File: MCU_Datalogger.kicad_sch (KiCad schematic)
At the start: 0 parts

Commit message: Have added required symbols to schematic sheets
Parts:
- added BT1: Battery, symbol Device:Battery
- added C1, C2, C3, C4: C, symbol Device:C
- added C5: C_Polarized_US, symbol Device:C_Polarized_US
- added D1, D2: LED, symbol Device:LED
- added H1, H2, H3, H4: MountingHole, symbol Mechanical:MountingHole
- added R1, R2, R3, R4, R5, R6, R7: R_US, symbol Device:R_US
- added U1, U2: 24LC1025, symbol Memory_EEPROM:24LC1025
- added U3: ATMEGA328P-AU, ATMEGA328P-AU:QFP80P900X900X120-32N, symbol ATMEGA328P-AU:ATMEGA328P-AU
- added U4: DS1337S_, DS1337S_:SOIC127P600X175-8N, symbol DS1337S_:DS1337S_
- added Y1, Y2: Crystal, symbol Device:Crystal
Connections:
- new net: U3.21 (GND), U3.3 (GND), U3.5 (GND)
- new net: U3.4 (VCC), U3.6 (VCC)
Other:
- added sheet Connectors (connectors.kicad_sch)
- title: (none) -> ${project_name}

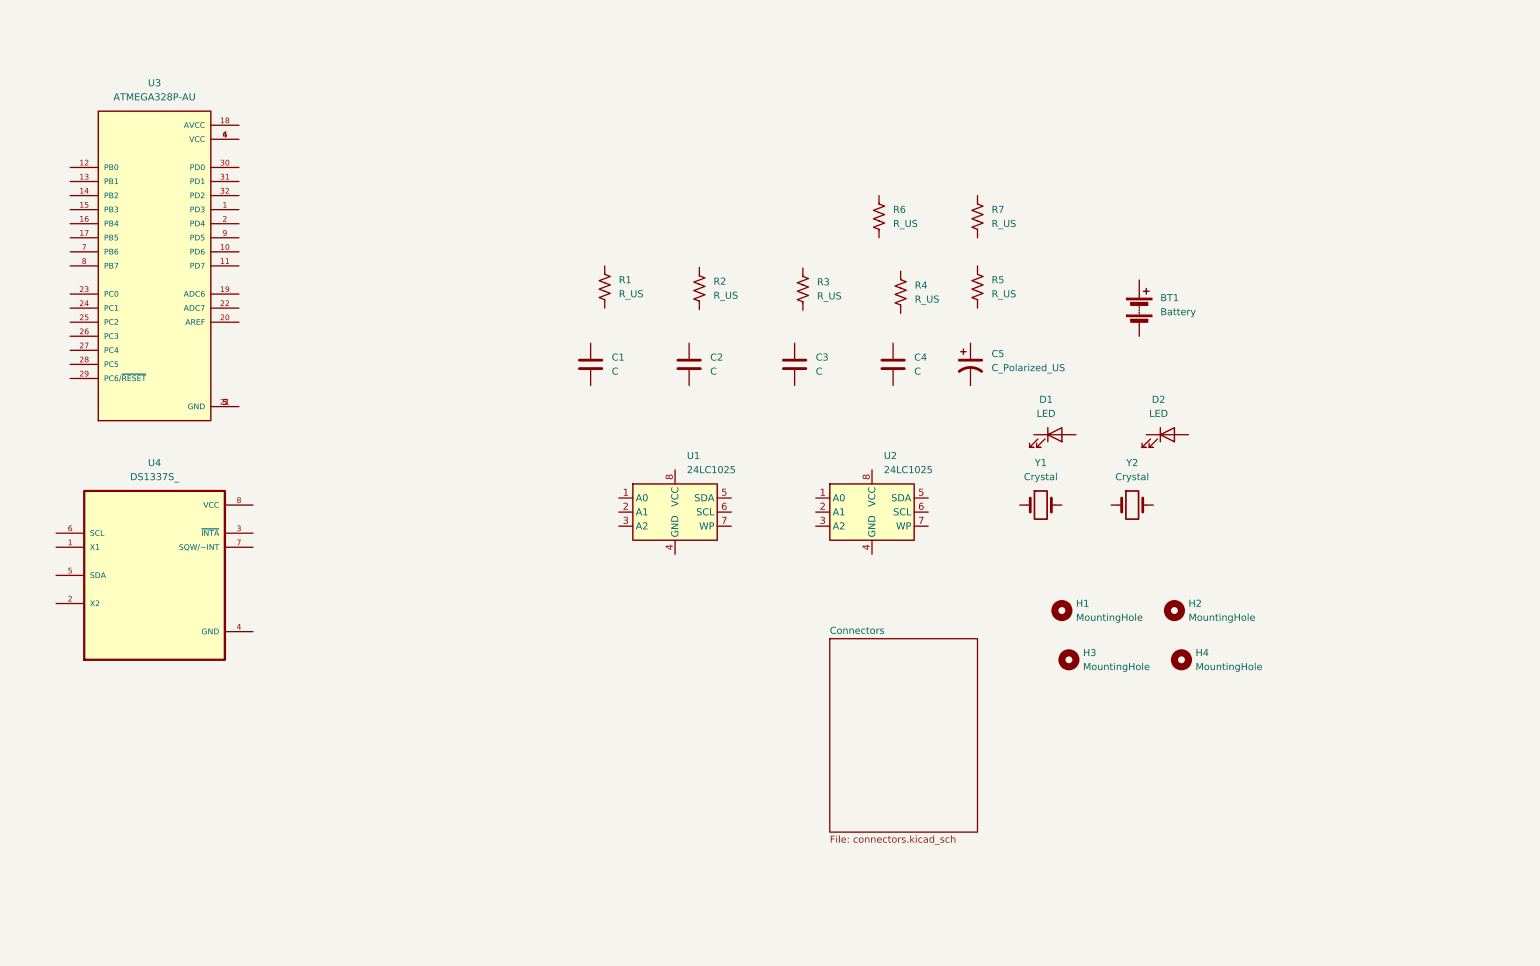
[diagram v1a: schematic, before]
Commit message: Changed the location of the symbols (arrange)
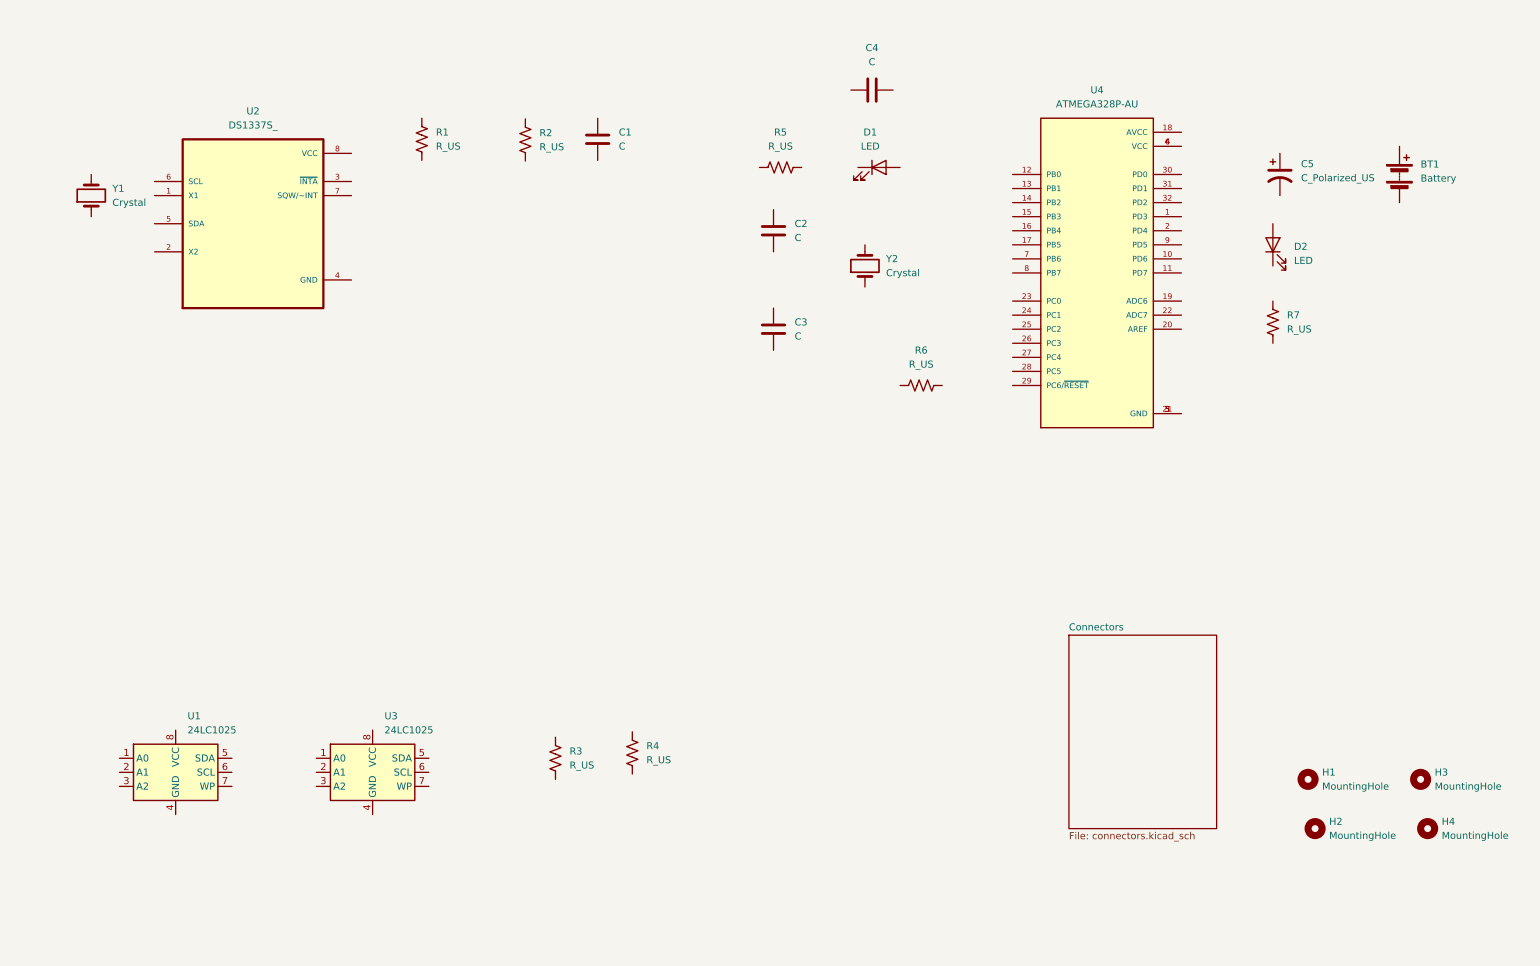
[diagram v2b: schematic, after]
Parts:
- renumbered C2 to C1, C3 to C2, C4 to C3, C1 to C4, D2 to D1, D1 to D2, H3 to H2, H2 to H3, R2 to R1, R3 to R2, R4 to R3, R5 to R4, R1 to R5, R7 to R6, R6 to R7, U4 to U2, U2 to U3, U3 to U4
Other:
- moved on the sheet: BT1, C1, C2, C3, C4, C5, D1, D2, H1, H2, H3, H4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

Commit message: Upated components with values
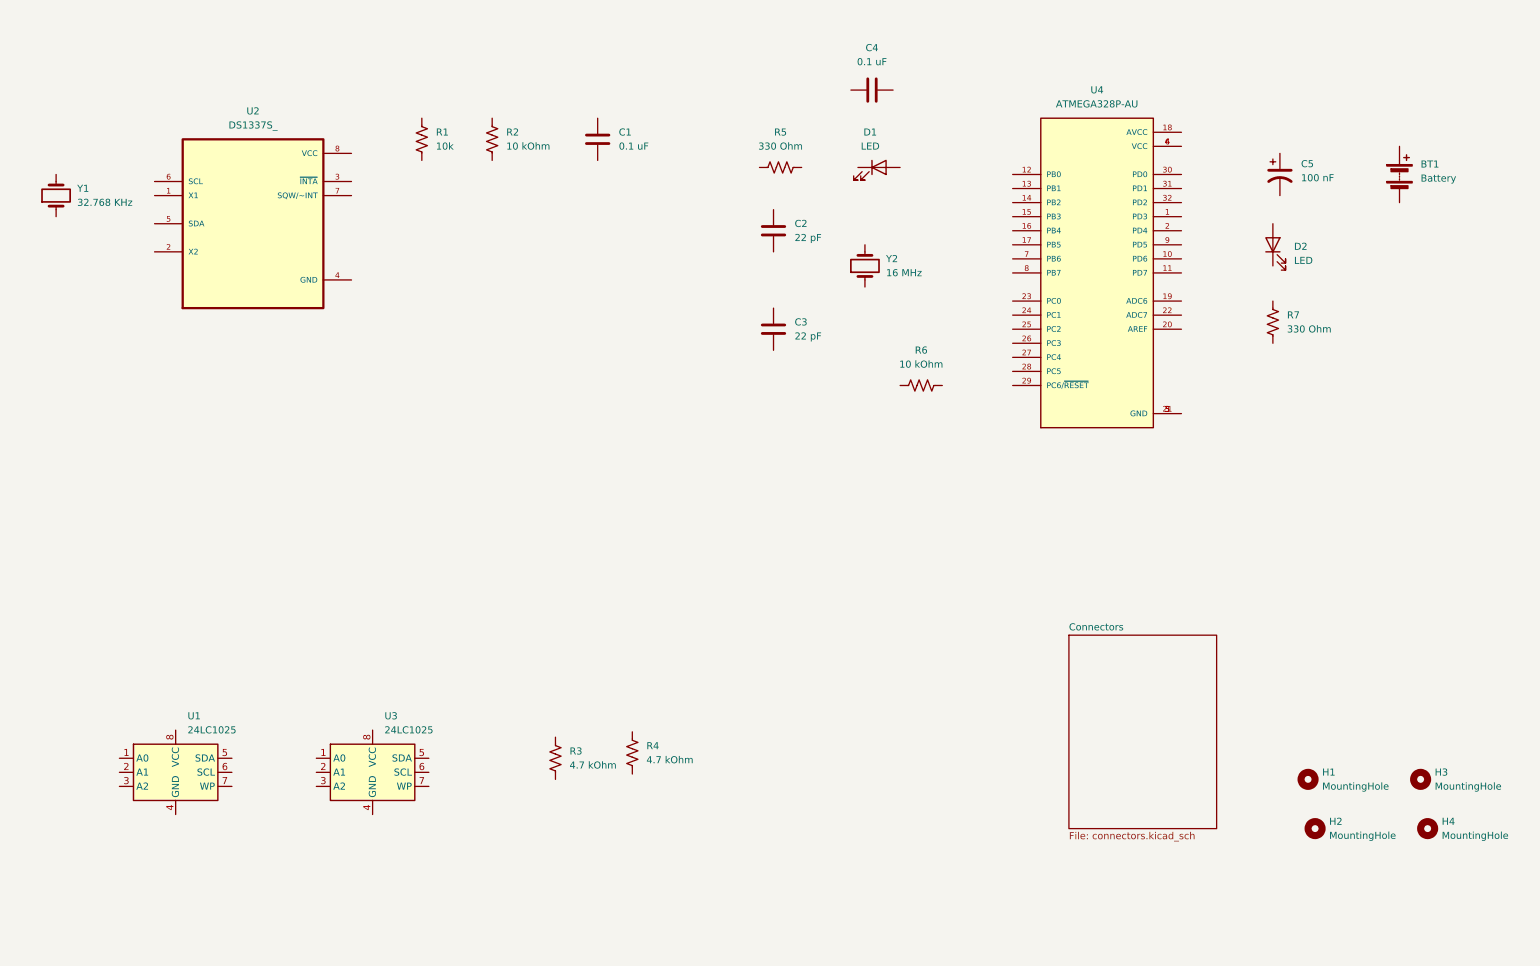
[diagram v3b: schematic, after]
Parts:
- C1, C4: value C -> 0.1 uF
- C2, C3: value C -> 22 pF
- C5: value C_Polarized_US -> 100 nF
- R1: value R_US -> 10k
- R2, R6: value R_US -> 10 kOhm
- R3, R4: value R_US -> 4.7 kOhm
- R5, R7: value R_US -> 330 Ohm
- Y1: value Crystal -> 32.768 KHz
- Y2: value Crystal -> 16 MHz
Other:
- moved on the sheet: R2, Y1
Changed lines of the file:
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@@
 			)
 		)
-		(property "Value" "R_US"
+		(property "Value" "4.7 kOhm"
 			(at 115.57 149.8599 0)
 			(effects
@@
 			)
 		)
+		(property "Purpose" ""
+			(at 113.03 148.59 0)
+			(effects
+				(font
+					(size 1.27 1.27)
+				)
+			)
+		)
 		(pin "2"
 		)
@@
 			)
 		)
-		(property "Value" "C"
+		(property "Value" "22 pF"
 			(at 156.21 54.6099 0)
 			(effects
@@
 			)
 		)
+		(property "Purpose" ""
+			(at 152.4 53.34 0)
+			(effects
+				(font
+					(size 1.27 1.27)
+				)
+			)
+		)
 		(pin "1"
 		)
@@
 			)
 		)
-		(property "Value" "R_US"
+		(property "Value" "10 kOhm"
 			(at 179.07 77.47 90)
 			(effects
@@
 			)
 		)
+		(property "Purpose" ""
+			(at 179.07 81.28 0)
+			(effects
+				(font
+					(size 1.27 1.27)
+				)
+			)
+		)
 		(pin "2"
 		)
@@
 			)
 		)
-		(property "Value" "R_US"
+		(property "Value" "4.7 kOhm"
 			(at 129.4466 148.9018 0)
 			(effects
@@
 			)
 		)
+		(property "Purpose" ""
+			(at 126.9066 147.6319 0)
+			(effects
+				(font
+					(size 1.27 1.27)
+				)
+			)
+		)
 		(pin "2"
 		)
@@
 	(symbol
 		(lib_id "Device:Crystal")
-		(at 29.21 46.99 90)
+		(at 22.86 46.99 90)
 		(unit 1)
 		(exclude_from_sim no)
@@
 		(fields_autoplaced yes)
 		(property "Reference" "Y1"
-			(at 33.02 45.7199 90)
+			(at 26.67 45.7199 90)
 			(effects
 				(font
@@
 			)
 		)
-		(property "Value" "Crystal"
-			(at 33.02 48.2599 90)
+		(property "Value" "32.768 KHz"
+			(at 26.67 48.2599 90)
 			(effects
 				(font
@@
 		)
 		(property "Footprint" ""
-			(at 29.21 46.99 0)
-			(effects
-				(font
-					(size 1.27 1.27)
-				)
-				(hide yes)
-			)
-		)
-		(property "Datasheet" "~"
-			(at 29.21 46.99 0)
+			(at 22.86 46.99 0)
+			(effects
+				(font
+					(size 1.27 1.27)
+				)
+				(hide yes)
+			)
+		)
+		(property "Datasheet" "~"
+			(at 22.86 46.99 0)
 			(effects
 				(font
@@
 		)
 		(property "Description" "Two pin crystal"
-			(at 29.21 46.99 0)
-			(effects
-				(font
-					(size 1.27 1.27)
-				)
-				(hide yes)
+			(at 22.86 46.99 0)
+			(effects
+				(font
+					(size 1.27 1.27)
+				)
+				(hide yes)
+			)
+		)
+		(property "Purpose" ""
+			(at 22.86 46.99 0)
+			(effects
+				(font
+					(size 1.27 1.27)
+				)
 			)
 		)
@@
 	(symbol
 		(lib_id "Device:R_US")
-		(at 107.5941 36.9462 0)
+		(at 101.6 36.83 0)
 		(unit 1)
 		(exclude_from_sim no)
@@
 		(fields_autoplaced yes)
 		(property "Reference" "R2"
-			(at 110.1341 35.6761 0)
-			(effects
-				(font
-					(size 1.27 1.27)
-				)
-				(justify left)
-			)
-		)
-		(property "Value" "R_US"
-			(at 110.1341 38.2161 0)
-			(effects
-				(font
-					(size 1.27 1.27)
-				)
-				(justify left)
-			)
-		)
-		(property "Footprint" ""
-			(at 108.6101 37.2002 90)
-			(effects
-				(font
-					(size 1.27 1.27)
-				)
-				(hide yes)
-			)
-		)
-		(property "Datasheet" "~"
-			(at 107.5941 36.9462 0)
+			(at 104.14 35.5599 0)
+			(effects
+				(font
+					(size 1.27 1.27)
+				)
+				(justify left)
+			)
+		)
+		(property "Value" "10 kOhm"
+			(at 104.14 38.0999 0)
+			(effects
+				(font
+					(size 1.27 1.27)
+				)
+				(justify left)
+			)
+		)
+		(property "Footprint" ""
+			(at 102.616 37.084 90)
+			(effects
+				(font
+					(size 1.27 1.27)
+				)
+				(hide yes)
+			)
+		)
+		(property "Datasheet" "~"
+			(at 101.6 36.83 0)
 			(effects
 				(font
@@
 		)
 		(property "Description" "Resistor, US symbol"
-			(at 107.5941 36.9462 0)
-			(effects
-				(font
-					(size 1.27 1.27)
-				)
-				(hide yes)
+			(at 101.6 36.83 0)
+			(effects
+				(font
+					(size 1.27 1.27)
+				)
+				(hide yes)
+			)
+		)
+		(property "Purpose" ""
+			(at 101.6 36.83 0)
+			(effects
+				(font
+					(size 1.27 1.27)
+				)
 			)
 		)
@@
 			)
 		)
-		(property "Value" "C"
+		(property "Value" "22 pF"
 			(at 156.21 72.3899 0)
 			(effects
@@
 			)
 		)
+		(property "Purpose" ""
+			(at 152.4 71.12 0)
+			(effects
+				(font
+					(size 1.27 1.27)
+				)
+			)
+		)
 		(pin "1"
 		)
@@
 			)
 		)
-		(property "Value" "C_Polarized_US"
+		(property "Value" "100 nF"
 			(at 247.65 43.8149 0)
 			(effects
@@
 			)
 		)
+		(property "Purpose" ""
+			(at 243.84 43.18 0)
+			(effects
+				(font
+					(size 1.27 1.27)
+				)
+			)
+		)
 		(pin "2"
 		)
@@
 			)
 		)
-		(property "Value" "R_US"
+		(property "Value" "10k"
 			(at 91.44 38.0999 0)
 			(effects
@@
 			)
 		)
+		(property "Purpose" ""
+			(at 88.9 36.83 0)
+			(effects
+				(font
+					(size 1.27 1.27)
+				)
+			)
+		)
 		(pin "2"
 		)
@@
 			)
 		)
-		(property "Value" "C"
+		(property "Value" "0.1 uF"
 			(at 170.18 22.86 90)
 			(effects
@@
 			)
 		)
+		(property "Purpose" ""
+			(at 170.18 27.94 0)
+			(effects
+				(font
+					(size 1.27 1.27)
+				)
+			)
+		)
 		(pin "1"
 		)
@@
 			)
 		)
-		(property "Value" "C"
+		(property "Value" "0.1 uF"
 			(at 124.46 38.0999 0)
 			(effects
@@
 			)
 		)
+		(property "Purpose" ""
+			(at 120.65 36.83 0)
+			(effects
+				(font
+					(size 1.27 1.27)
+				)
+			)
+		)
 		(pin "1"
 		)
@@
 			)
 		)
-		(property "Value" "Crystal"
+		(property "Value" "16 MHz"
 			(at 172.72 60.9599 90)
 			(effects
@@
 			)
 		)
+		(property "Purpose" ""
+			(at 168.91 59.69 0)
+			(effects
+				(font
+					(size 1.27 1.27)
+				)
+			)
+		)
 		(pin "1"
 		)
@@
 			)
 		)
-		(property "Value" "R_US"
+		(property "Value" "330 Ohm"
 			(at 153.67 38.1 90)
 			(effects
@@
 			)
 		)
+		(property "Purpose" ""
+			(at 153.67 41.91 0)
+			(effects
+				(font
+					(size 1.27 1.27)
+				)
+			)
+		)
 		(pin "2"
 		)
@@
 			)
 		)
-		(property "Value" "R_US"
+		(property "Value" "330 Ohm"
 			(at 245.11 71.1199 0)
 			(effects
@@
 			)
 		)
+		(property "Purpose" ""
+			(at 242.57 69.85 0)
+			(effects
+				(font
+					(size 1.27 1.27)
+				)
+			)
+		)

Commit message: Added footprints to components in schematic and added external library for external footprints
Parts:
- BT1: footprint (none) -> Connector_PinHeader_2.54mm:PinHeader_1x02_P2.54mm_Vertical
- C1, C2, C3, C4, C5: footprint (none) -> Capacitor_SMD:C_0805_2012Metric
- D1, D2: footprint (none) -> LED_SMD:LED_0805_2012Metric
- H1, H2, H3, H4: footprint (none) -> MountingHole:MountingHole_2.1mm
- R1, R2, R3, R4, R5, R6, R7: footprint (none) -> Resistor_SMD:R_0805_2012Metric
- U1, U3: footprint (none) -> Package_SO:SOIC-8_5.3x5.3mm_P1.27mm
- U2: footprint DS1337S_:SOIC127P600X175-8N -> Footprints:SOIC127P600X175-8N
- U4: footprint ATMEGA328P-AU:QFP80P900X900X120-32N -> Footprints:QFP80P900X900X120-32N
- Y1, Y2: footprint (none) -> Crystal:Crystal_SMD_5032-2Pin_5.0x3.2mm_HandSoldering
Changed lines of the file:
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@@
 			)
 		)
-		(property "Footprint" "DS1337S_:SOIC127P600X175-8N"
+		(property "Footprint" "Footprints:SOIC127P600X175-8N"
 			(at 58.42 52.07 0)
 			(effects
@@
 			)
 		)
-		(property "Footprint" ""
+		(property "Footprint" "Resistor_SMD:R_0805_2012Metric"
 			(at 114.046 148.844 90)
 			(effects
@@
 			)
 		)
-		(property "Footprint" ""
+		(property "Footprint" "Capacitor_SMD:C_0805_2012Metric"
 			(at 153.3652 57.15 0)
 			(effects
@@
 			)
 		)
-		(property "Footprint" ""
+		(property "Footprint" "Connector_PinHeader_2.54mm:PinHeader_1x02_P2.54mm_Vertical"
 			(at 265.43 41.656 90)
 			(effects
@@
 			)
 		)
-		(property "Footprint" ""
+		(property "Footprint" "Resistor_SMD:R_0805_2012Metric"
 			(at 179.324 80.264 90)
 			(effects
@@
 			)
 		)
-		(property "Footprint" ""
+		(property "Footprint" "LED_SMD:LED_0805_2012Metric"
 			(at 242.57 55.88 0)
 			(effects
@@
 			)
 		)
-		(property "Footprint" ""
+		(property "Footprint" "Resistor_SMD:R_0805_2012Metric"
 			(at 127.9226 147.8859 90)
 			(effects
@@
 			)
 		)
-		(property "Footprint" "ATMEGA328P-AU:QFP80P900X900X120-32N"
+		(property "Footprint" "Footprints:QFP80P900X900X120-32N"
 			(at 210.82 60.96 0)
 			(effects
@@
 			)
 		)
-		(property "Footprint" ""
+		(property "Footprint" "MountingHole:MountingHole_2.1mm"
 			(at 250.19 161.29 0)
 			(effects
@@
 			)
 		)
-		(property "Footprint" ""
+		(property "Footprint" "Crystal:Crystal_SMD_5032-2Pin_5.0x3.2mm_HandSoldering"
 			(at 22.86 46.99 0)
 			(effects
@@
 			)
 		)
-		(property "Footprint" ""
+		(property "Footprint" "Resistor_SMD:R_0805_2012Metric"
 			(at 102.616 37.084 90)
 			(effects
@@
 			)
 		)
-		(property "Footprint" ""
+		(property "Footprint" "LED_SMD:LED_0805_2012Metric"
 			(at 171.45 41.91 0)
 			(effects
@@
 			)
 		)
-		(property "Footprint" ""
+		(property "Footprint" "Capacitor_SMD:C_0805_2012Metric"
 			(at 153.3652 74.93 0)
 			(effects
@@
 			)
 		)
-		(property "Footprint" ""
+		(property "Footprint" "Package_SO:SOIC-8_5.3x5.3mm_P1.27mm"
 			(at 80.01 151.13 0)
 			(effects
@@
 			)
 		)
-		(property "Footprint" ""
+		(property "Footprint" "MountingHole:MountingHole_2.1mm"
 			(at 248.92 152.4 0)
 			(effects
@@
 			)
 		)
-		(property "Footprint" ""
+		(property "Footprint" "Package_SO:SOIC-8_5.3x5.3mm_P1.27mm"
 			(at 44.45 151.13 0)
 			(effects
@@
 			)
 		)
-		(property "Footprint" ""
+		(property "Footprint" "Capacitor_SMD:C_0805_2012Metric"
 			(at 243.84 43.18 0)
 			(effects
@@
 			)
 		)
-		(property "Footprint" ""
+		(property "Footprint" "Resistor_SMD:R_0805_2012Metric"
 			(at 89.916 37.084 90)
 			(effects
@@
 			)
 		)
-		(property "Footprint" ""
+		(property "Footprint" "Capacitor_SMD:C_0805_2012Metric"
 			(at 173.99 26.9748 0)
 			(effects
@@
 			)
 		)
-		(property "Footprint" ""
+		(property "Footprint" "Capacitor_SMD:C_0805_2012Metric"
 			(at 121.6152 40.64 0)
 			(effects
@@
 			)
 		)
-		(property "Footprint" ""
+		(property "Footprint" "Crystal:Crystal_SMD_5032-2Pin_5.0x3.2mm_HandSoldering"
 			(at 168.91 59.69 0)
 			(effects
@@
 			)
 		)
-		(property "Footprint" ""
+		(property "Footprint" "MountingHole:MountingHole_2.1mm"
 			(at 270.51 161.29 0)
 			(effects
@@
 			)
 		)
-		(property "Footprint" ""
+		(property "Footprint" "MountingHole:MountingHole_2.1mm"
 			(at 269.24 152.4 0)
 			(effects
@@
 			)
 		)
-		(property "Footprint" ""
+		(property "Footprint" "Resistor_SMD:R_0805_2012Metric"
 			(at 153.924 40.894 90)
 			(effects
@@
 			)
 		)
-		(property "Footprint" ""
+		(property "Footprint" "Resistor_SMD:R_0805_2012Metric"
 			(at 243.586 70.104 90)
 			(effects
